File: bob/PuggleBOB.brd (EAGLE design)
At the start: 30.5 x 85.1 mm, 9 parts

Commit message: Finished BOB.
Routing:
- net DAC_C: track 35.2 -> 53.0 mm, vias 2 -> 0
- net DAC_B: track 51.9 -> 67.3 mm, vias 2 -> 0
- net DAC_D: track 21.5 -> 36.1 mm, vias 2 -> 0
- net DAC_A: track 68.7 -> 70.2 mm
- net ADC_C: track 35.7 -> 36.2 mm

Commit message: Minor changes.
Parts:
- moved AI_0 65.3 mm to (24.1, 10.2)
- moved AI_1 65.3 mm to (24.1, 27.9)
- moved AI_2 65.3 mm to (24.1, 45.7)
- moved AI_3 65.3 mm to (24.1, 63.5)
- moved AO_0 65.3 mm to (6.35, 10.2)
- moved AO_1 65.3 mm to (6.35, 27.9)
- moved AO_2 65.3 mm to (6.35, 45.7)
- moved AO_3 65.3 mm to (6.35, 63.5)
- moved A_I/O 62.8 mm to (15.2, 78.7)
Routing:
- net ADC_A: track 73.3 -> 70.8 mm
- net DAC_A: track 70.2 -> 67.7 mm
- net ADC_D: track 17.6 -> 15.0 mm
- net ADC_B: track 54.5 -> 51.9 mm
- net DAC_B: track 67.3 -> 64.7 mm
- net ADC_C: track 36.2 -> 33.6 mm
- net DAC_D: track 36.1 -> 33.7 mm
- net DAC_C: track 53.0 -> 50.9 mm
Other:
- board size 30.5 x 85.1 mm -> 30.5 x 82.5 mm
- board text added: "PuggleBOB Jon Newman v1.0"

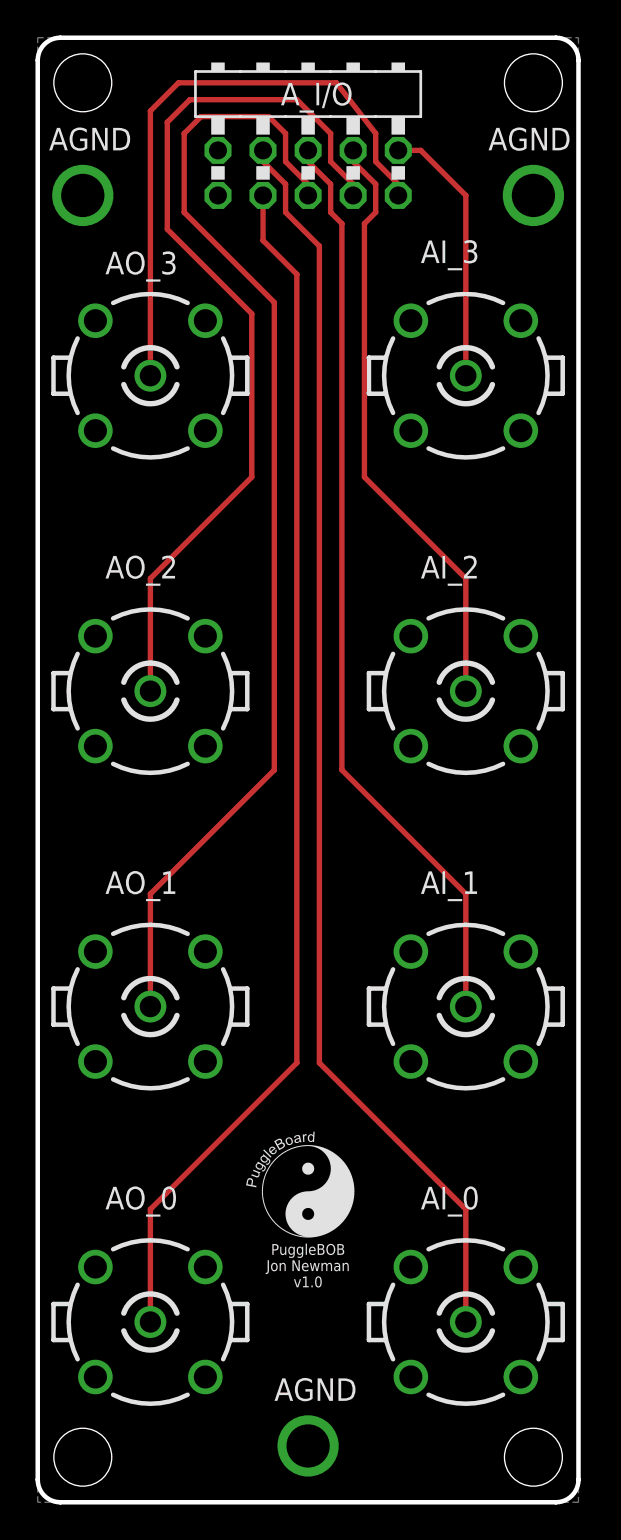
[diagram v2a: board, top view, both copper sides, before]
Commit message: Fixed the ribbon cable mapping to take into account reflective symmetry.
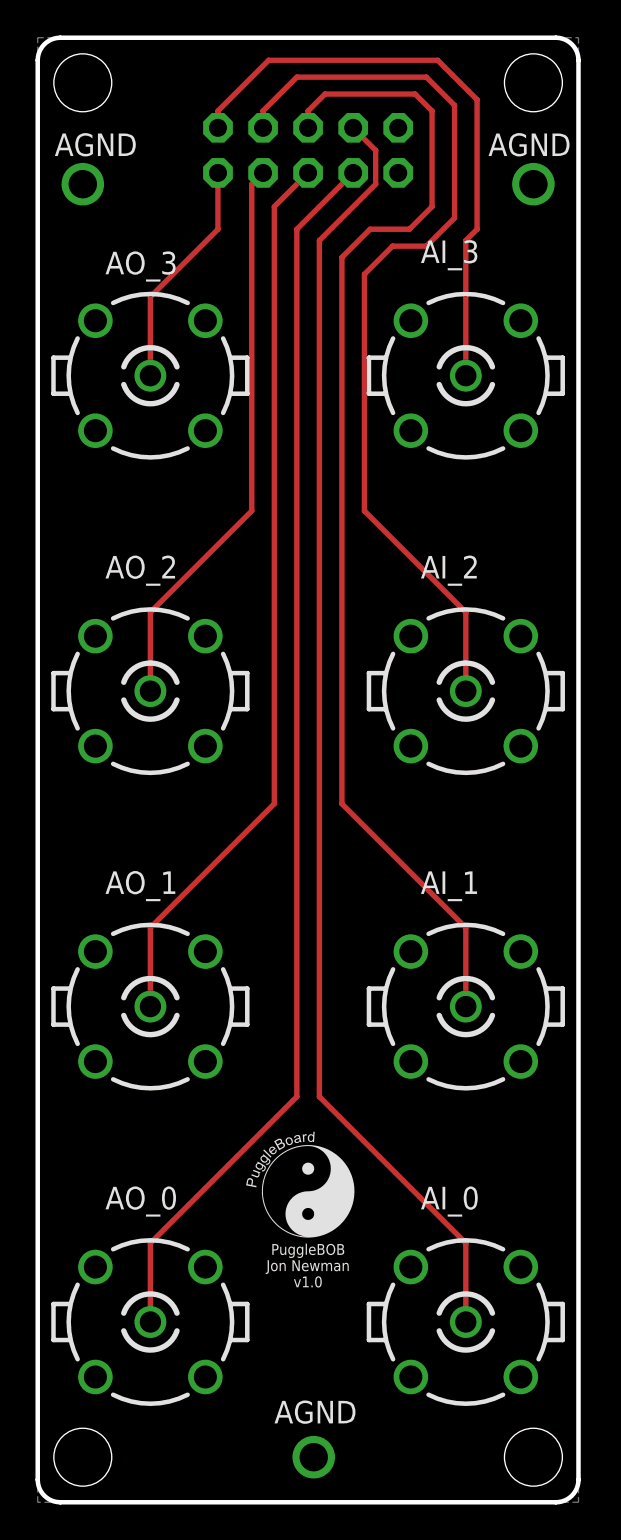
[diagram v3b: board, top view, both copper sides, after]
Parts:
- A_I/O: value PINHD-2X5/90 -> PINHD-2X5; device adafruit:2X05/90 -> adafruit:2X05
- moved A_I/O 2.54 mm to (15.2, 76.2), flipped to the bottom
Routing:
- net DAC_D: track 33.7 -> 13.0 mm
- net DAC_C: track 50.9 -> 31.8 mm
- net ADC_D: track 15.0 -> 33.5 mm
- net ADC_C: track 33.6 -> 51.8 mm
- net DAC_B: track 64.7 -> 50.7 mm
- net ADC_B: track 51.9 -> 65.5 mm
- net DAC_A: track 67.7 -> 69.5 mm
- net ADC_A: track 70.8 -> 72.6 mm
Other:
- board text added: "0"
- board text added: "1"
- board text added: "2"
- board text added: "3"
- board text added: "ADC"
- board text added: "DAC"

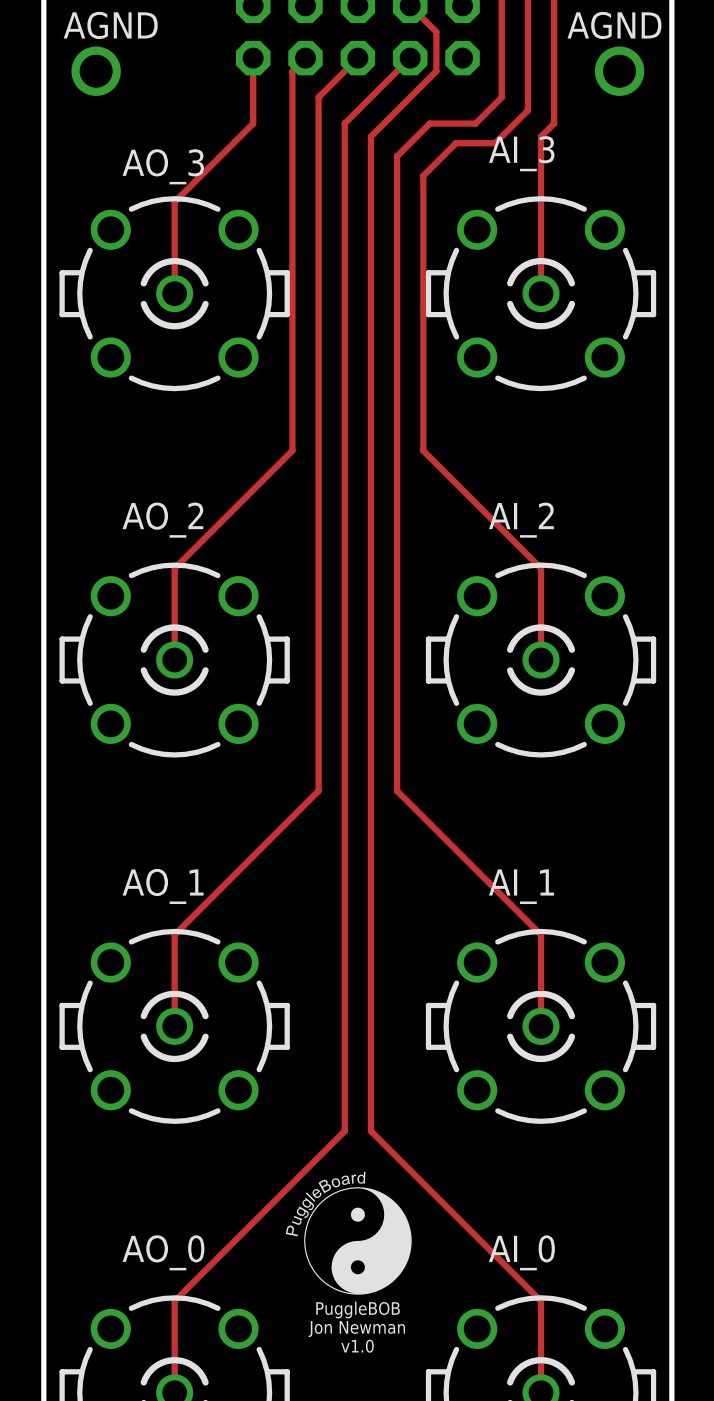
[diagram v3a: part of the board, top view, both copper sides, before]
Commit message: Silkscreen changes.
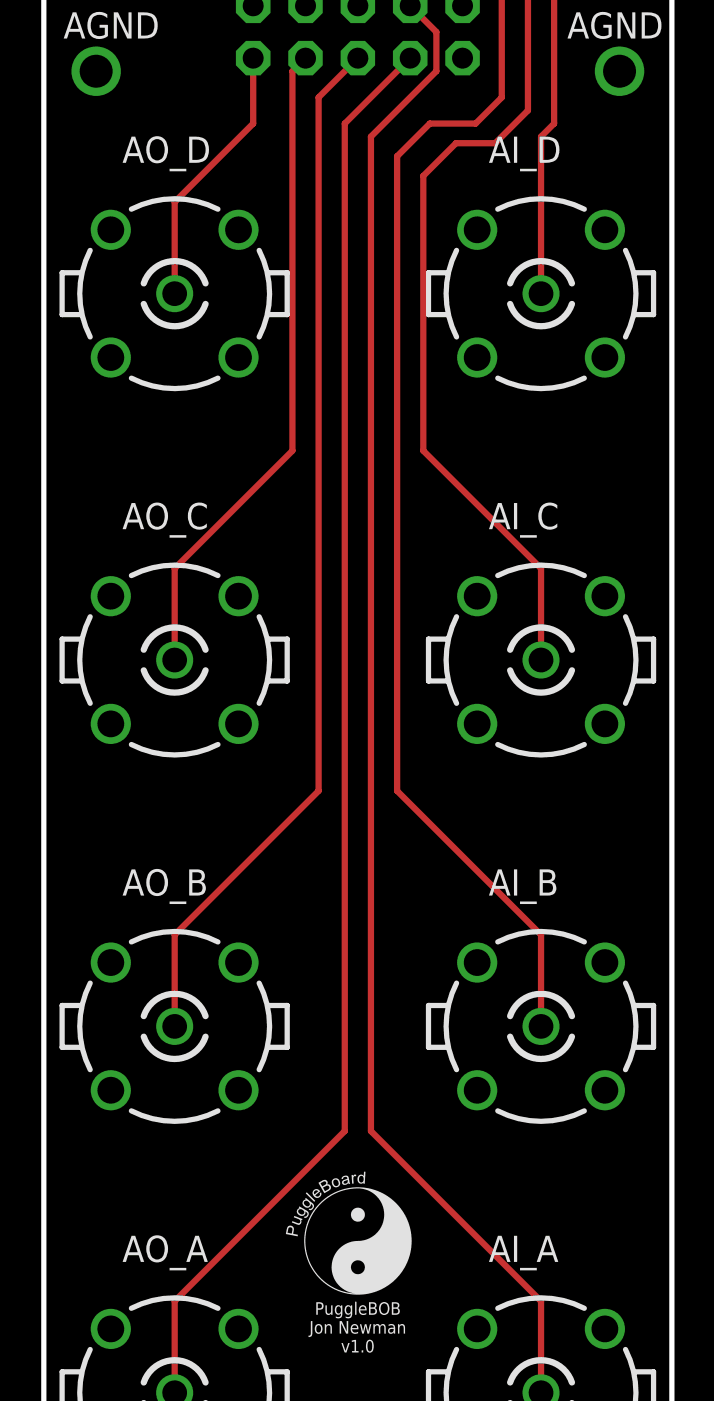
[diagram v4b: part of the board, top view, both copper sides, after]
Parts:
- renumbered AI_0 to AI_A, AI_1 to AI_B, AI_2 to AI_C, AI_3 to AI_D, AO_0 to AO_A, AO_1 to AO_B, AO_2 to AO_C, AO_3 to AO_D
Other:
- board text added: "A"
- board text added: "B"
- board text added: "C"
- board text added: "D"
- board text removed: "0"
- board text removed: "1"
- board text removed: "2"
- board text removed: "3"

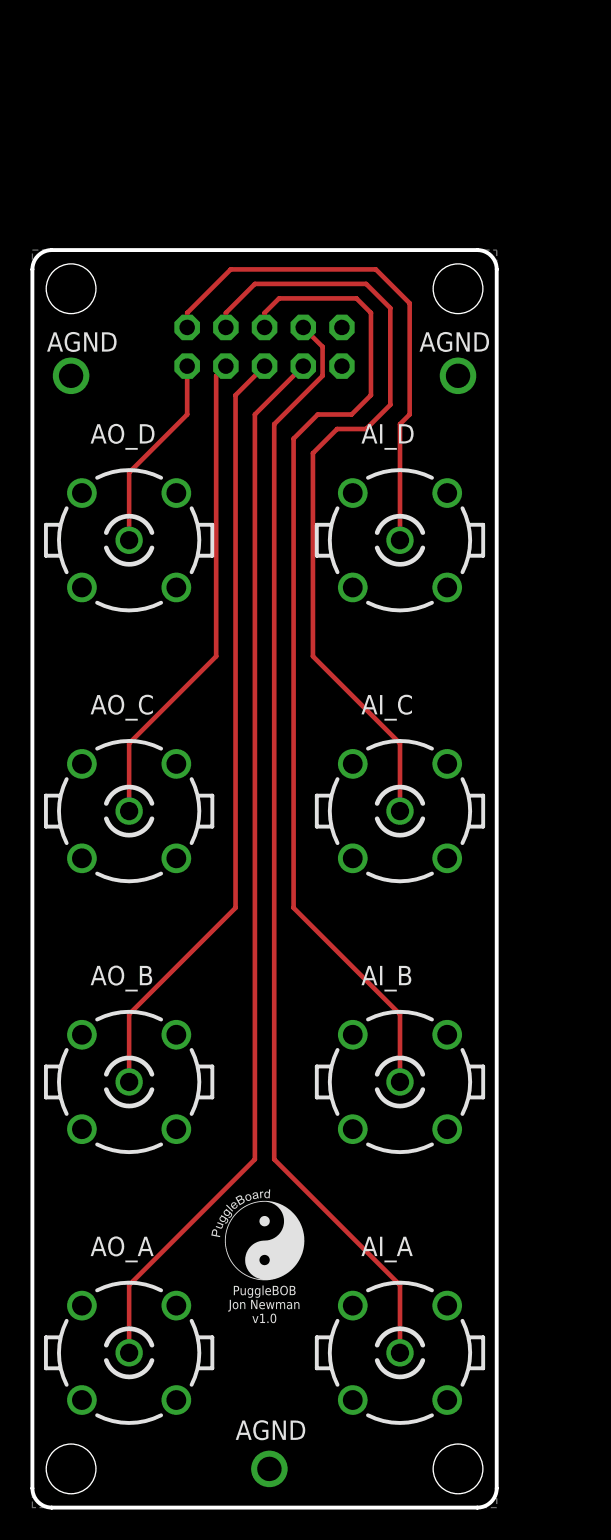
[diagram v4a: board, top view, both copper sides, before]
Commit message: Ready to print v0.1
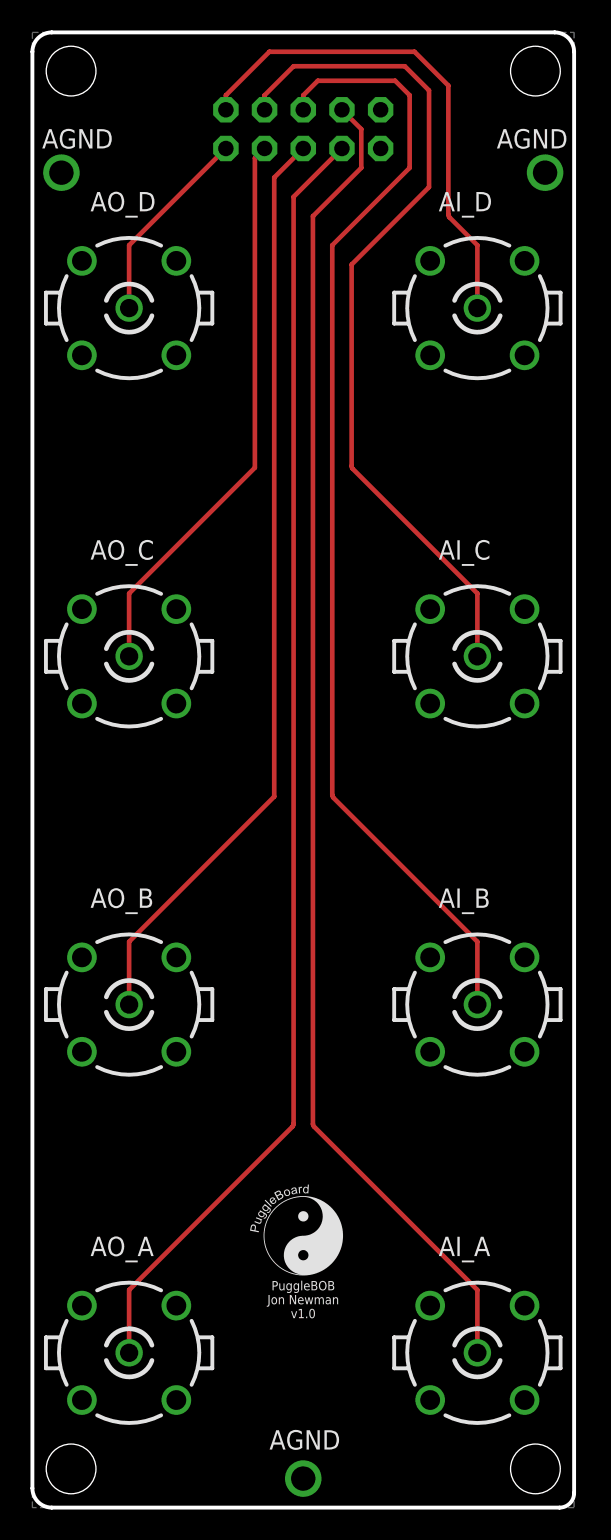
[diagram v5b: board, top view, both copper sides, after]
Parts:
- moved AI_D 16.1 mm to (29.2, 78.7)
- moved AO_D 15.2 mm to (6.35, 78.7)
- moved A_I/O 14.5 mm to (17.8, 90.5)
- moved AI_C 11.4 mm to (29.2, 55.9)
- moved AO_C 10.2 mm to (6.35, 55.9)
- moved AI_B 7.18 mm to (29.2, 33.0)
- moved AI_A 5.08 mm to (29.2, 10.2)
- moved AO_B 5.08 mm to (6.35, 33.0)
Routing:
- net DAC_A: track 69.5 -> 84.8 mm
- net ADC_A: track 72.6 -> 87.9 mm
- net DAC_B: track 50.7 -> 60.9 mm
- net ADC_B: track 65.5 -> 74.5 mm
- net DAC_C: track 31.8 -> 37.0 mm
- net ADC_C: track 51.8 -> 55.8 mm
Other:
- board size 30.5 x 82.5 mm -> 35.6 x 96.8 mm
